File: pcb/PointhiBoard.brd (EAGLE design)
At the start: 110 x 60 mm, 105 parts, among them IC1 MCP7940N, IC2 ADP2303ARDZ-5.0, IC3 IRF7240, IC4 IRF7240, IC5 18F4420, IC6 4052D, IC7 ADR02, J1 22-27-2021-02, Q1 BSS123, Q2 BSS123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

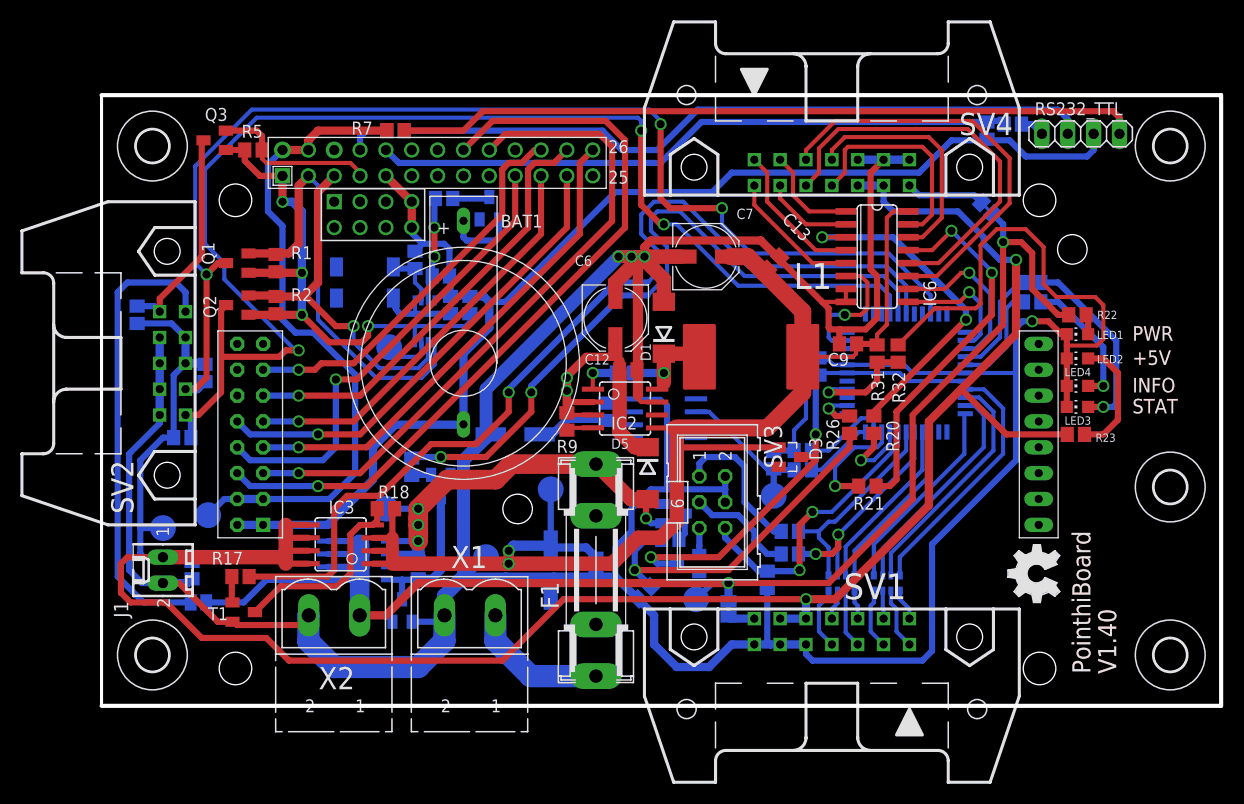
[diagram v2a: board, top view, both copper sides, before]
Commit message: fix hole-diameter of con-harting-ml
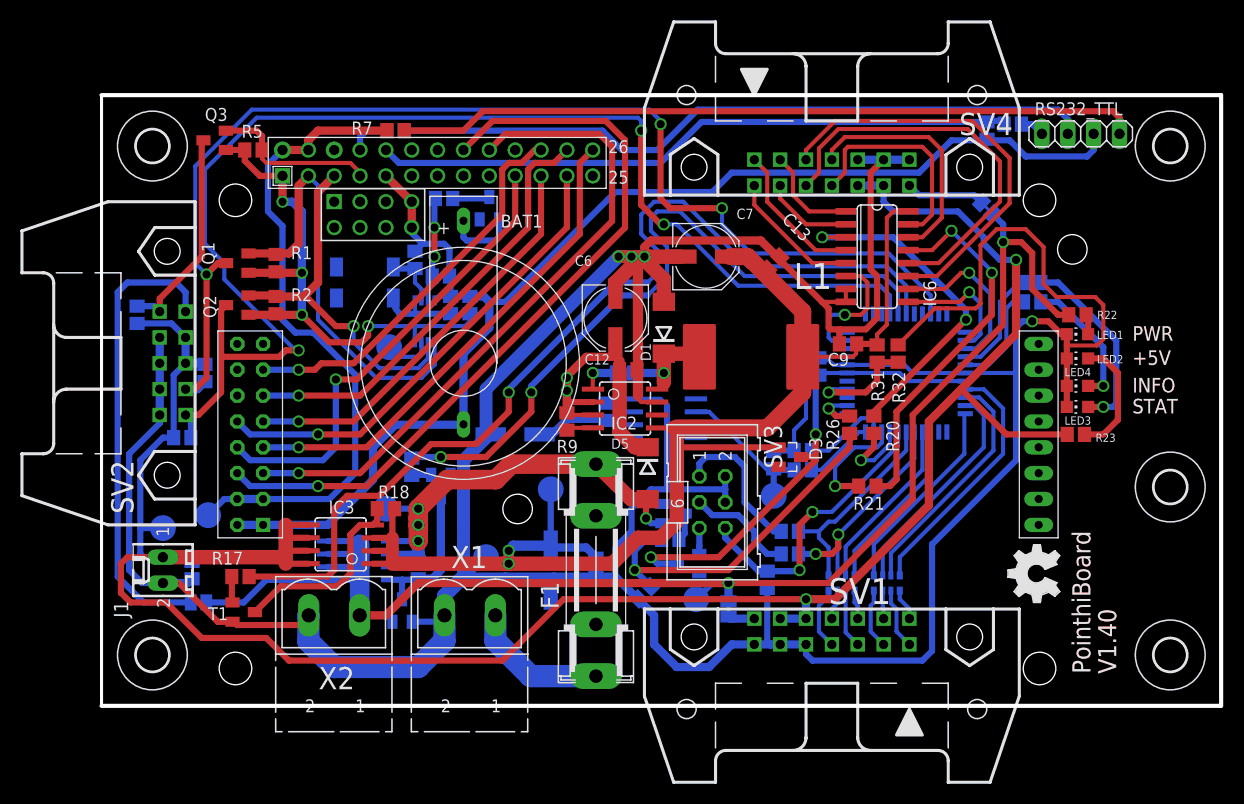
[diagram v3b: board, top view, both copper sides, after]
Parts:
- SV1: value (none) -> D-IO; device con-harting-ml:3M_14L -> con-harting-ml-mod:3M_14L
- SV2: device con-harting-ml:3M_10L -> con-harting-ml-mod:3M_10L
- SV4: value (none) -> ADC-IN; device con-harting-ml:3M_14L -> con-harting-ml-mod:3M_14L
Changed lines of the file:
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@@
 <layer number="49" name="Reference" color="7" fill="1" visible="no" active="yes"/>
 <layer number="50" name="dxf" color="7" fill="1" visible="no" active="yes"/>
-<layer number="51" name="tDocu" color="7" fill="1" visible="yes" active="yes"/>
-<layer number="52" name="bDocu" color="7" fill="1" visible="yes" active="yes"/>
+<layer number="51" name="tDocu" color="7" fill="1" visible="no" active="yes"/>
+<layer number="52" name="bDocu" color="7" fill="1" visible="no" active="yes"/>
 <layer number="53" name="tGND_GNDA" color="7" fill="1" visible="no" active="yes"/>
 <layer number="54" name="bGND_GNDA" color="7" fill="1" visible="no" active="yes"/>
@@
 <elements>
 <element name="U$1" library="RaspberryPi" package="RASPBERRY-PI_REV2" value="RASPBERRY-PI_REV2" x="59.69" y="30.48" locked="yes" smashed="yes"/>
-<element name="SV2" library="con-harting-ml" package="3M_10L" value="I2C" x="3.175" y="33.655" smashed="yes" rot="R90">
+<element name="SV2" library="con-harting-ml-mod" package="3M_10L" value="I2C" x="3.175" y="33.655" smashed="yes" rot="R90">
 <attribute name="OC_NEWARK" value="unknown" x="3.175" y="33.655" size="1.778" layer="27" rot="R90" display="off"/>
 <attribute name="MPN" value="" x="3.175" y="33.655" size="1.778" layer="27" rot="R90" display="off"/>
@@
 <attribute name="VALUE" x="88.36025" y="23.3124" size="1.778" layer="28" rot="MR0"/>
 </element>
-<element name="SV1" library="con-harting-ml" package="3M_14L" value="" x="71.755" y="3.4925" smashed="yes" rot="R180">
+<element name="SV1" library="con-harting-ml-mod" package="3M_14L" value="D-IO" x="71.755" y="3.4925" smashed="yes" rot="R180">
 <attribute name="OC_NEWARK" value="unknown" x="71.755" y="3.4925" size="1.778" layer="27" rot="R180" display="off"/>
 <attribute name="MPN" value="" x="71.755" y="3.4925" size="1.778" layer="27" rot="R180" display="off"/>
 <attribute name="MF" value="" x="71.755" y="3.4925" size="1.778" layer="27" rot="R180" display="off"/>
 <attribute name="OC_FARNELL" value="unknown" x="71.755" y="3.4925" size="1.778" layer="27" rot="R180" display="off"/>
-<attribute name="NAME" x="79.0575" y="13.0175" size="2.54" layer="25" rot="R180"/>
-<attribute name="VALUE" x="66.675" y="13.6525" size="2.54" layer="27" rot="R180"/>
+<attribute name="NAME" x="71.4375" y="10.00125" size="2.54" layer="25"/>
+<attribute name="VALUE" x="80.48625" y="10.16" size="2.54" layer="27"/>
 </element>
 <element name="SJ2" library="jumper" package="SJ" value="" x="61.595" y="9.525" smashed="yes" rot="MR270">
@@
 <attribute name="VALUE" x="68.707" y="18.19275" size="1.016" layer="28" rot="MR0"/>
 </element>
-<element name="SV4" library="con-harting-ml" package="3M_14L" value="" x="71.755" y="56.1975" smashed="yes">
+<element name="SV4" library="con-harting-ml-mod" package="3M_14L" value="ADC-IN" x="71.755" y="56.1975" smashed="yes">
 <attribute name="OC_NEWARK" value="unknown" x="71.755" y="56.1975" size="1.778" layer="27" display="off"/>
 <attribute name="MPN" value="" x="71.755" y="56.1975" size="1.778" layer="27" display="off"/>
@@
 <attribute name="OC_FARNELL" value="unknown" x="71.755" y="56.1975" size="1.778" layer="27" display="off"/>
 <attribute name="NAME" x="89.535" y="58.26125" size="2.1844" layer="25" rot="R180"/>
-<attribute name="VALUE" x="76.835" y="46.0375" size="2.54" layer="27"/>
+<attribute name="VALUE" x="90.805" y="51.7525" size="2.1844" layer="27"/>
 </element>
 <element name="IC6" library="40xx" package="SO16" value="4052D" x="76.2" y="44.1325" smashed="yes" rot="R270">

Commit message: fix warnings on pcb
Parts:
- Q4: value (none) -> 32.768KHZ
- SV3: value (none) -> ICSP
- SV5: value (none) -> RS232_TTL
- X1: value (none) -> VCC-IN
- X2: value (none) -> VCC-OUT
- moved R24 0.35 mm to (87.3, 56.4)
- moved R10 0.32 mm to (89.9, 57.1)
- moved R6 0.16 mm to (3.49, 38.3)
- renumbered 32.768KHZ to Q4, RS232_TTL to SV5
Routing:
- net GND1: track 132.9 -> 133.5 mm
